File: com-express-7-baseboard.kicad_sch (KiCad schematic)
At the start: 0 parts

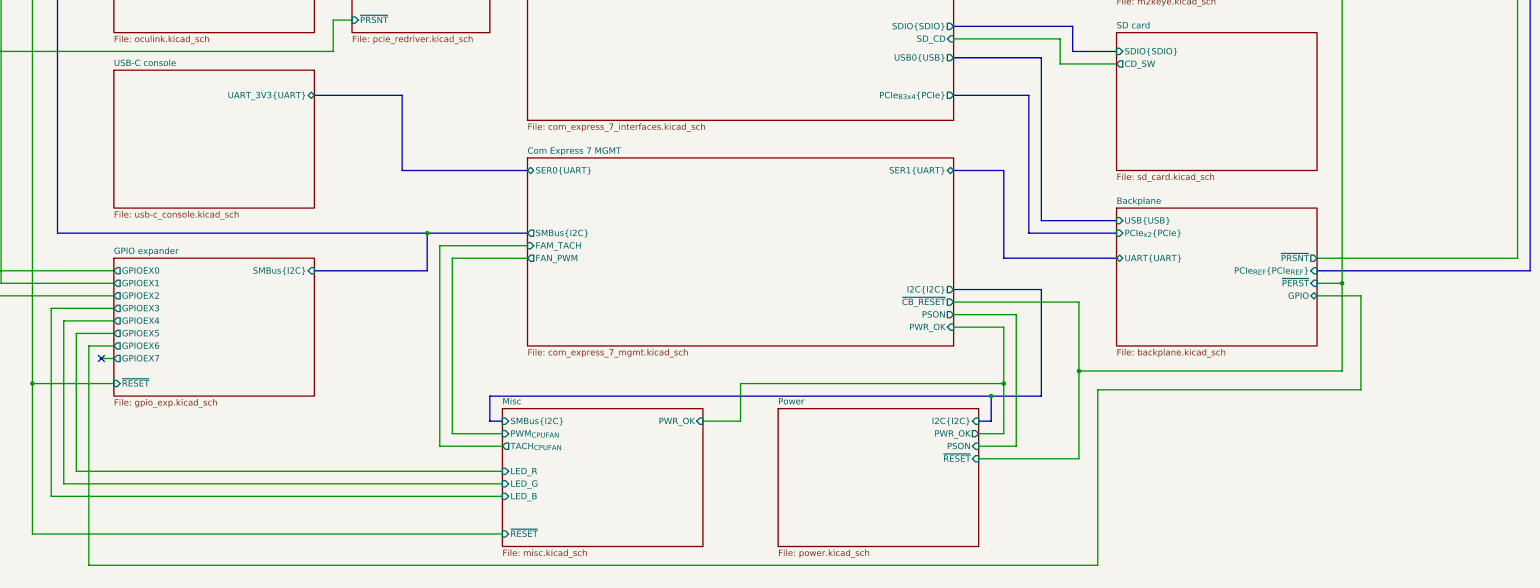
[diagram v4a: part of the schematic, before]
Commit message: [#58904] Fix DRC
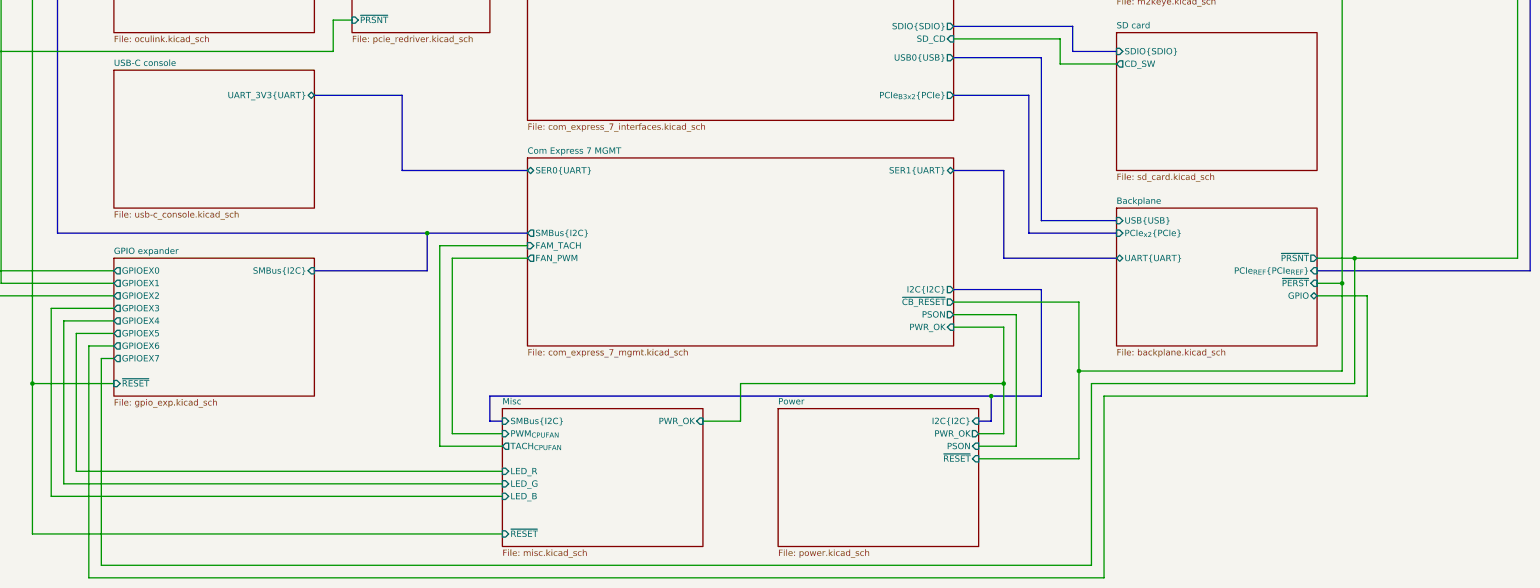
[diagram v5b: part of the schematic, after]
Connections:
- no-connect marks 1 -> 0
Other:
- sheet Com Express 7 Interfaces ports: added PCIe_{B3x2}{PCIe}; removed PCIe_{B3x4}{PCIe}
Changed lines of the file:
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@@
   (junction (at 327.66 104.14) (diameter 0) (color 0 0 0 0)
   )
+  (junction (at 330.2 213.36) (diameter 0) (color 0 0 0 0)
+  )
   (junction (at 325.12 101.6) (diameter 0) (color 0 0 0 0)
   )
@@
   (junction (at 62.23 144.78) (diameter 0) (color 0 0 0 0)
   )
-  (no_connect (at 76.2 233.68))
   (bus (pts (xy 259.08 213.36) (xy 281.94 213.36))
     (stroke (width 0) (type default) (color 255 153 0 1))
@@
     (stroke (width 0) (type default) (color 255 0 0 1))
   )
-  (wire (pts (xy 278.13 240.03) (xy 331.47 240.03))
+  (wire (pts (xy 279.4 241.3) (xy 332.74 241.3))
     (stroke (width 0) (type default))
   )
@@
     (stroke (width 0) (type default))
   )
-  (wire (pts (xy 278.13 275.59) (xy 278.13 240.03))
-    (stroke (width 0) (type default))
-  )
-  (wire (pts (xy 322.58 213.36) (xy 363.22 213.36))
+  (wire (pts (xy 279.4 278.13) (xy 279.4 241.3))
+    (stroke (width 0) (type default))
+  )
+  (wire (pts (xy 322.58 213.36) (xy 330.2 213.36))
     (stroke (width 0) (type default))
   )
@@
     (stroke (width 0) (type default))
   )
-  (wire (pts (xy 331.47 240.03) (xy 331.47 220.98))
+  (wire (pts (xy 332.74 241.3) (xy 332.74 220.98))
     (stroke (width 0) (type default))
   )
@@
   )
   (wire (pts (xy 119.38 86.36) (xy 121.92 86.36))
+    (stroke (width 0) (type default))
+  )
+  (wire (pts (xy 276.86 238.76) (xy 330.2 238.76))
     (stroke (width 0) (type default))
   )
@@
     (stroke (width 0) (type default))
   )
+  (wire (pts (xy 76.2 233.68) (xy 76.2 275.59))
+    (stroke (width 0) (type default))
+  )
+  (wire (pts (xy 276.86 275.59) (xy 276.86 238.76))
+    (stroke (width 0) (type default))
+  )
   (wire (pts (xy 327.66 46.99) (xy 62.23 46.99))
     (stroke (width 0) (type default))
@@
     (stroke (width 0) (type default))
   )
+  (wire (pts (xy 330.2 238.76) (xy 330.2 213.36))
+    (stroke (width 0) (type default))
+  )
   (bus (pts (xy 154.94 241.3) (xy 256.54 241.3))
     (stroke (width 0) (type default))
@@
     (stroke (width 0) (type default))
   )
-  (wire (pts (xy 73.66 231.14) (xy 73.66 275.59))
+  (wire (pts (xy 73.66 231.14) (xy 73.66 278.13))
+    (stroke (width 0) (type default))
+  )
+  (wire (pts (xy 330.2 213.36) (xy 363.22 213.36))
     (stroke (width 0) (type default))
   )
@@
     (stroke (width 0) (type default))
   )
-  (wire (pts (xy 73.66 275.59) (xy 278.13 275.59))
+  (wire (pts (xy 73.66 278.13) (xy 279.4 278.13))
     (stroke (width 0) (type default))
   )
@@
     (stroke (width 0) (type default))
   )
+  (wire (pts (xy 76.2 275.59) (xy 276.86 275.59))
+    (stroke (width 0) (type default))
+  )
   (wire (pts (xy 259.08 248.92) (xy 254 248.92))
     (stroke (width 0) (type default))
@@
     (stroke (width 0) (type default) (color 194 0 194 1))
   )
-  (wire (pts (xy 331.47 220.98) (xy 322.58 220.98))
+  (wire (pts (xy 332.74 220.98) (xy 322.58 220.98))
     (stroke (width 0) (type default))
   )
@@
       (effects (font (size 1.27 1.27)) (justify left))
     )
-    (pin "PCIe_{B3x4}{PCIe}" output (at 248.92 180.34 0)
-      (effects (font (size 1.27 1.27)) (justify right))
-    )
+    (pin "PCIe_{B3x2}{PCIe}" output (at 248.92 180.34 0)
+      (effects (font (size 1.27 1.27)) (justify right))
+    )

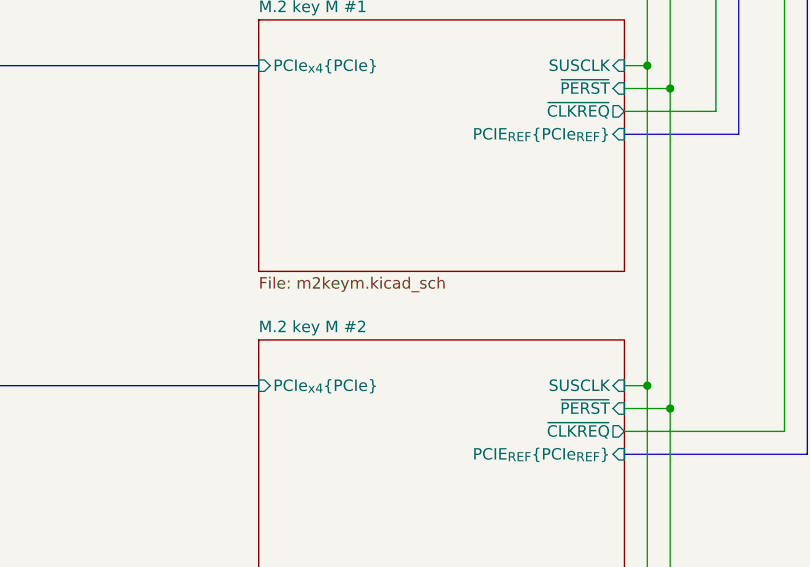
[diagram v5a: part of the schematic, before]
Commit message: [#65446] Add low profile M.2 key M connector, move M.2 drives
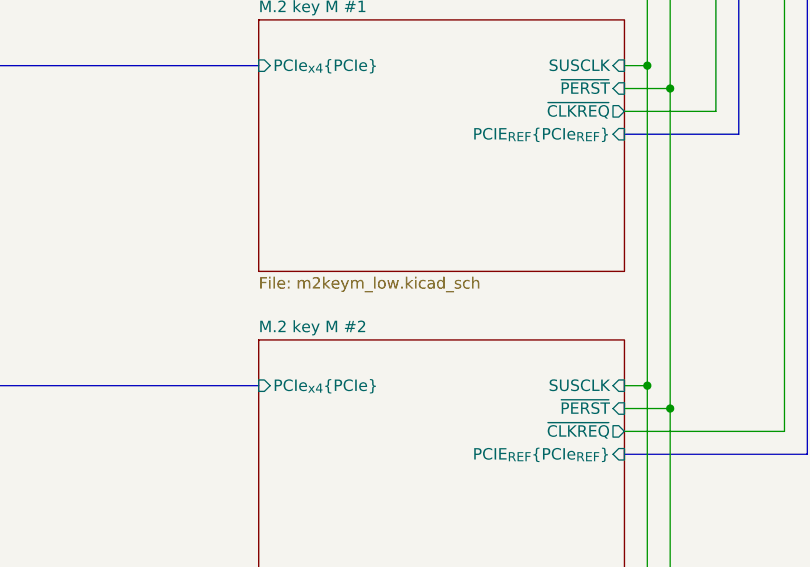
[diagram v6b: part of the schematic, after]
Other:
- sheet M.2 key M #1: file m2keym.kicad_sch -> m2keym_low.kicad_sch
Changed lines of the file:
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@@
       (effects (font (size 1.27 1.27)) (justify left bottom))
     )
-    (property "Sheetfile" "m2keym.kicad_sch" (at 281.94 89.4846 0)
+    (property "Sheetfile" "m2keym_low.kicad_sch" (at 281.94 89.4846 0)
       (effects (font (size 1.27 1.27)) (justify left top))
     )

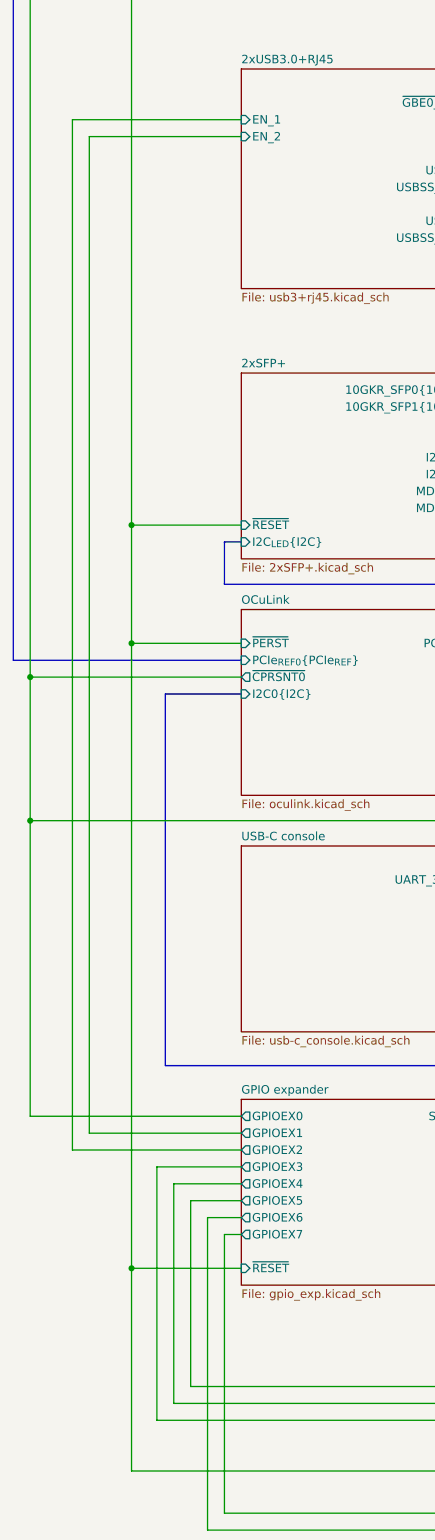
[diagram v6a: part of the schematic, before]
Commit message: [#66234] Adjust ESD protection diodes, layout fan connectors
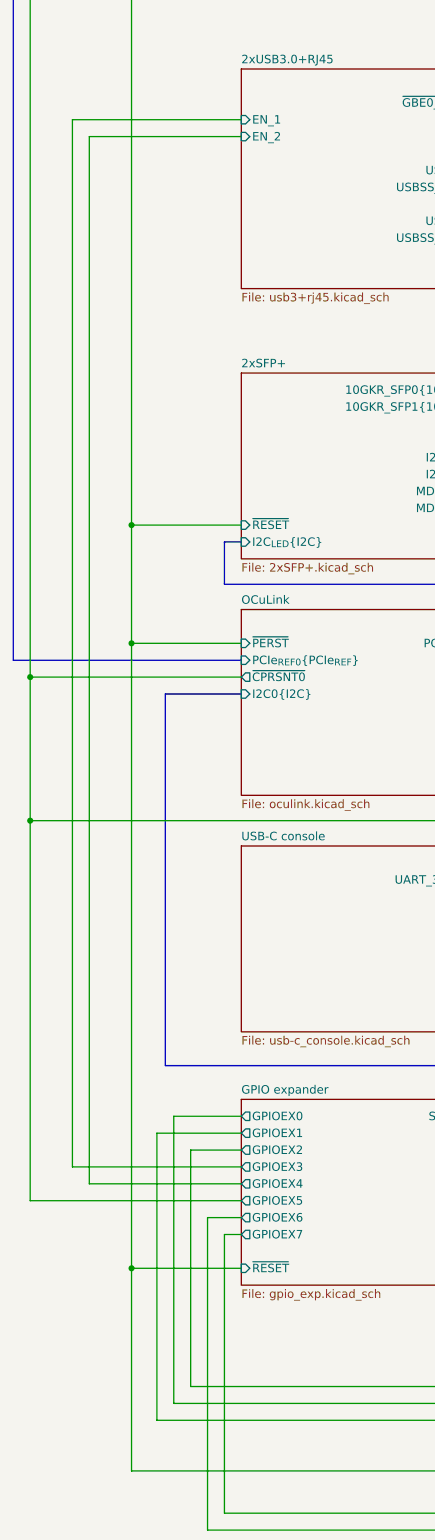
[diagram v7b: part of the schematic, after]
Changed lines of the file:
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@@
-    (stroke (width 0) (type default))
-  )
-  (wire (pts (xy 46.99 171.45) (xy 46.99 215.9))
     (stroke (width 0) (type default))
   )
@@
     (stroke (width 0) (type default))
   )
+  (wire (pts (xy 46.99 171.45) (xy 46.99 228.6))
+    (stroke (width 0) (type default))
+  )
   (bus (pts (xy 335.28 73.66) (xy 335.28 35.56))
     (stroke (width 0) (type default))
@@
   )
   (wire (pts (xy 281.94 173.99) (xy 270.51 173.99))
+    (stroke (width 0) (type default))
+  )
+  (wire (pts (xy 66.04 218.44) (xy 66.04 261.62))
     (stroke (width 0) (type default))
   )
@@
     (stroke (width 0) (type default) (color 0 0 255 1))
   )
-  (wire (pts (xy 78.74 223.52) (xy 66.04 223.52))
+  (wire (pts (xy 55.88 226.06) (xy 78.74 226.06))
+    (stroke (width 0) (type default))
+  )
+  (wire (pts (xy 71.12 220.98) (xy 71.12 256.54))
+    (stroke (width 0) (type default))
+  )
+  (wire (pts (xy 46.99 228.6) (xy 78.74 228.6))
     (stroke (width 0) (type default))
   )
@@
   )
   (wire (pts (xy 270.51 173.99) (xy 270.51 168.91))
-    (stroke (width 0) (type default))
-  )
-  (wire (pts (xy 71.12 256.54) (xy 71.12 228.6))
     (stroke (width 0) (type default))
   )
@@
     (stroke (width 0) (type default))
   )
-  (wire (pts (xy 78.74 218.44) (xy 55.88 218.44))
-    (stroke (width 0) (type default))
-  )
   (wire (pts (xy 322.58 142.24) (xy 355.6 142.24))
     (stroke (width 0) (type default))
@@
     (stroke (width 0) (type default))
   )
-  (wire (pts (xy 71.12 228.6) (xy 78.74 228.6))
-    (stroke (width 0) (type default))
-  )
   (wire (pts (xy 198.12 246.38) (xy 205.74 246.38))
     (stroke (width 0) (type default))
@@
     (stroke (width 0) (type default))
   )
-  (wire (pts (xy 55.88 68.58) (xy 55.88 218.44))
-    (stroke (width 0) (type default))
-  )
-  (wire (pts (xy 78.74 215.9) (xy 46.99 215.9))
+  (wire (pts (xy 55.88 68.58) (xy 55.88 226.06))
     (stroke (width 0) (type default))
   )
@@
     (stroke (width 0) (type default))
   )
-  (wire (pts (xy 66.04 223.52) (xy 66.04 261.62))
-    (stroke (width 0) (type default))
-  )
   (wire (pts (xy 66.04 261.62) (xy 157.48 261.62))
     (stroke (width 0) (type default))
@@
     (stroke (width 0) (type default))
   )
-  (wire (pts (xy 53.34 66.04) (xy 53.34 220.98))
+  (wire (pts (xy 53.34 66.04) (xy 53.34 223.52))
     (stroke (width 0) (type default))
   )
@@
     (stroke (width 0) (type default))
   )
+  (wire (pts (xy 68.58 215.9) (xy 68.58 259.08))
+    (stroke (width 0) (type default))
+  )
   (wire (pts (xy 325.12 101.6) (xy 325.12 66.04))
     (stroke (width 0) (type default))
@@
     (stroke (width 0) (type default))
   )
-  (wire (pts (xy 68.58 259.08) (xy 68.58 226.06))
-    (stroke (width 0) (type default))
-  )
   (bus (pts (xy 254 35.56) (xy 261.62 35.56))
     (stroke (width 0) (type default))
@@
     (stroke (width 0) (type default))
   )
-  (wire (pts (xy 68.58 226.06) (xy 78.74 226.06))
+  (wire (pts (xy 66.04 218.44) (xy 78.74 218.44))
     (stroke (width 0) (type default))
   )
@@
     (stroke (width 0) (type default))
   )
+  (wire (pts (xy 78.74 215.9) (xy 68.58 215.9))
+    (stroke (width 0) (type default))
+  )
   (wire (pts (xy 254 254) (xy 274.32 254))
     (stroke (width 0) (type default))
@@
     (stroke (width 0) (type default))
   )
+  (wire (pts (xy 78.74 220.98) (xy 71.12 220.98))
+    (stroke (width 0) (type default))
+  )
   (wire (pts (xy 119.38 88.9) (xy 121.92 88.9))
     (stroke (width 0) (type default))
@@
     (stroke (width 0) (type default) (color 194 0 194 1))
   )
+  (wire (pts (xy 78.74 223.52) (xy 53.34 223.52))
+    (stroke (width 0) (type default))
+  )
   (wire (pts (xy 327.66 218.44) (xy 327.66 139.7))
     (stroke (width 0) (type default))
@@
     (stroke (width 0) (type default))
   )
-  (wire (pts (xy 78.74 220.98) (xy 53.34 220.98))
-    (stroke (width 0) (type default))
-  )
